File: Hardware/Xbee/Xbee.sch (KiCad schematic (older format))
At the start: 39 parts, among them J1 Alimentación, J2 Raspberry, J3 Pines 1, J4 Pines 2, J5 Programación, J6 Entrada, J7 Salida, K1 Rele12V, Q2 BC338, Q3 BC338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

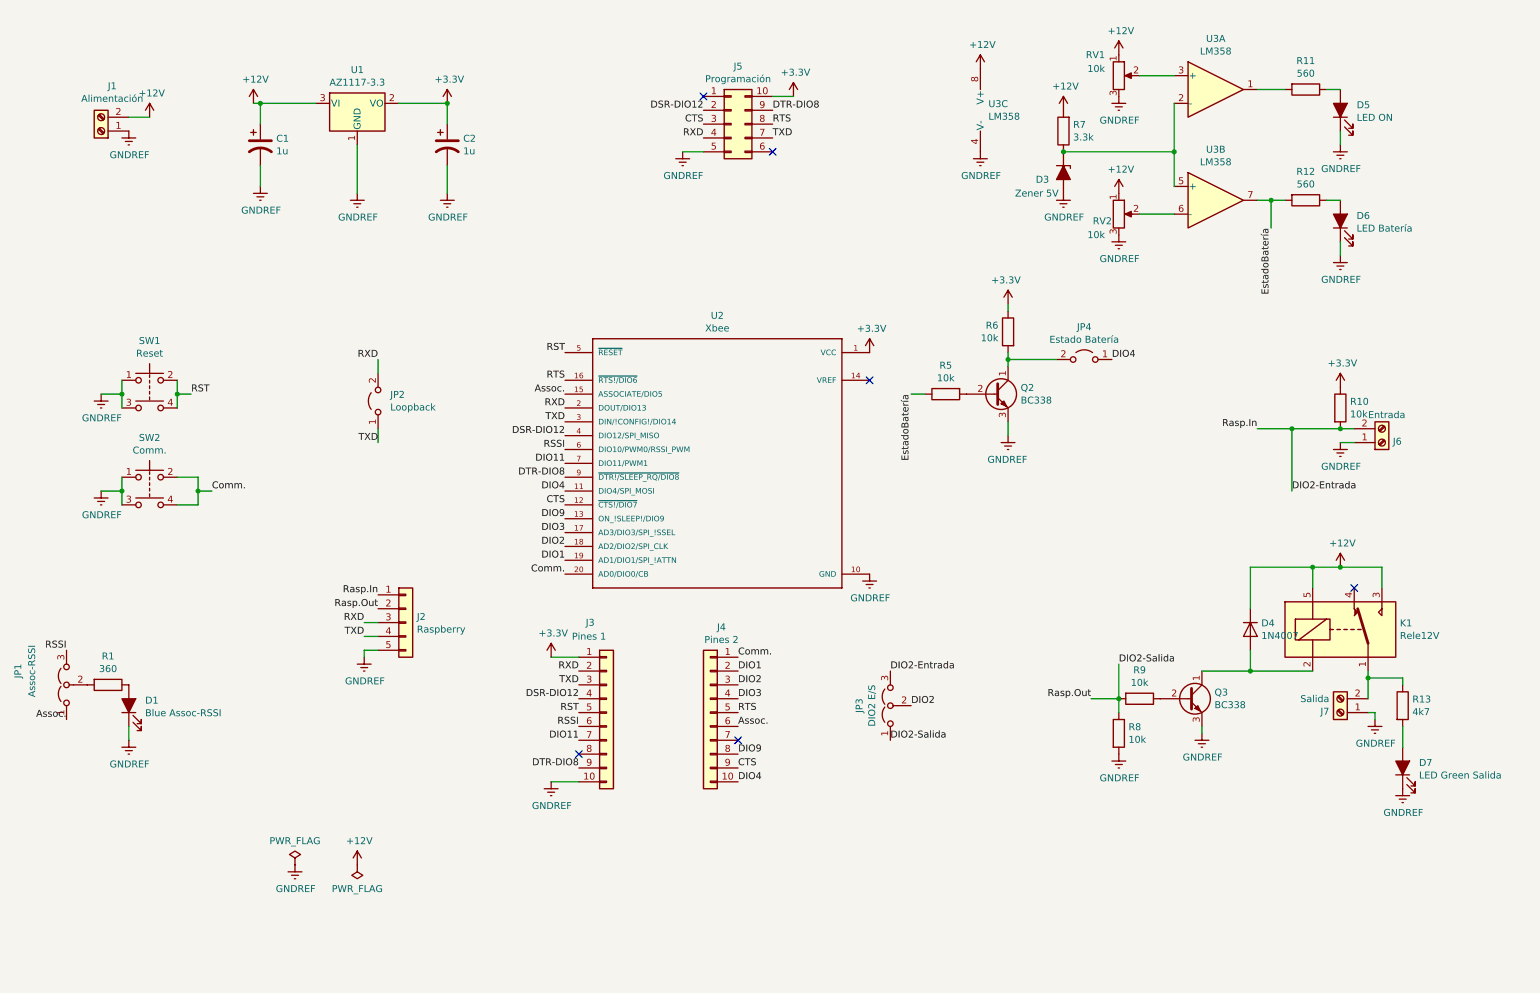
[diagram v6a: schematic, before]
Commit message: MOSFET, R SMD
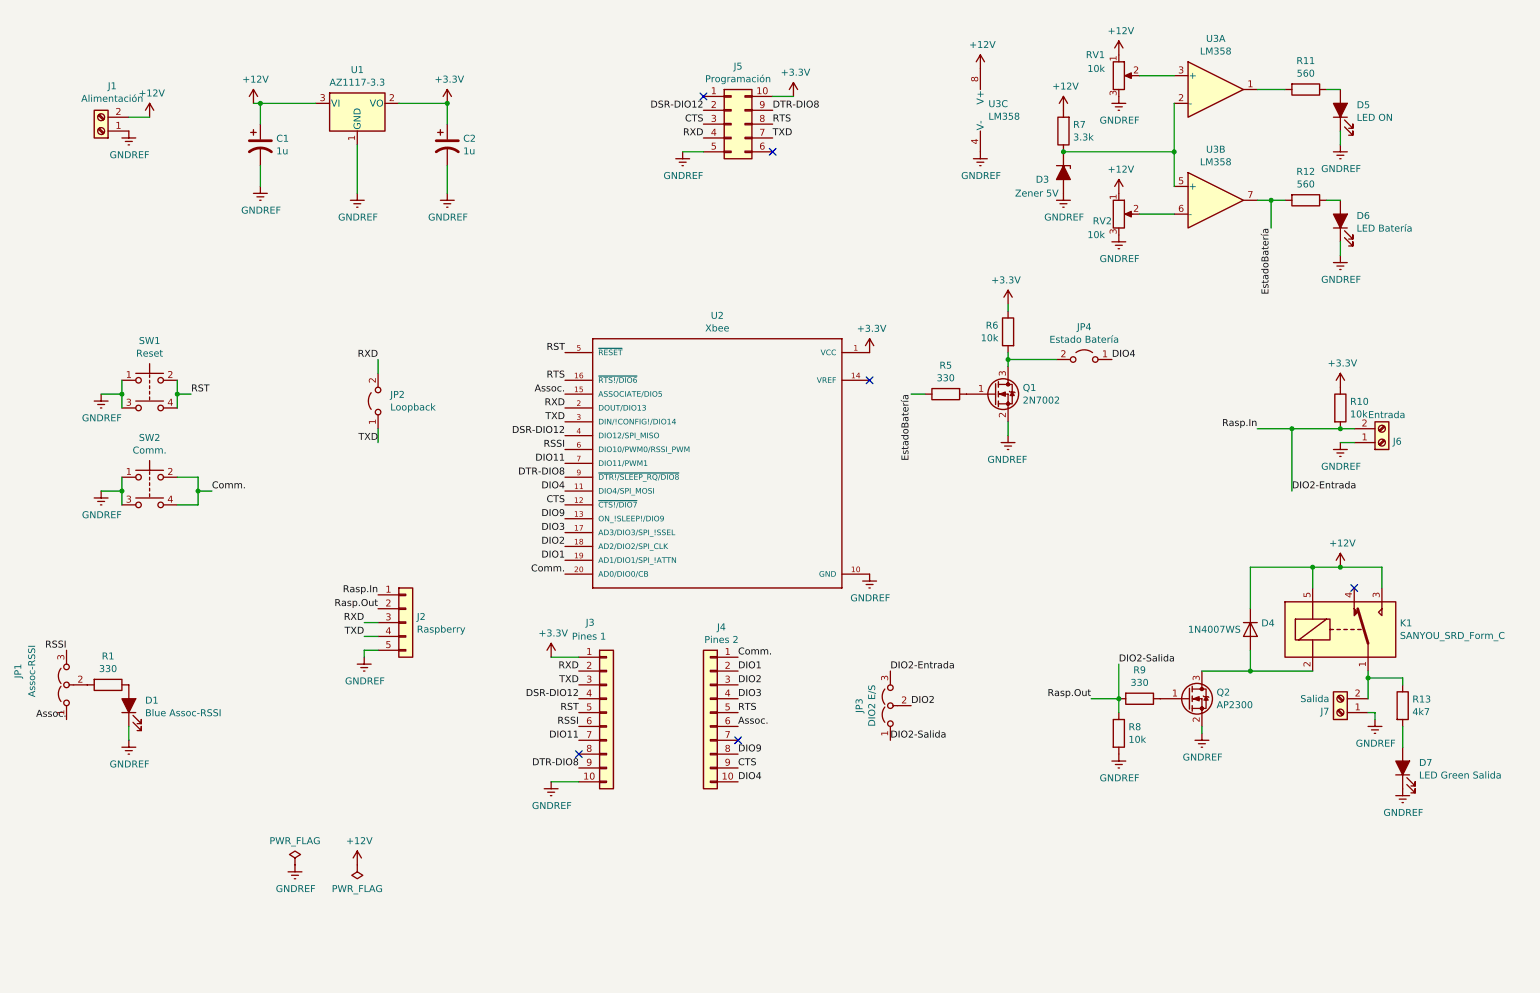
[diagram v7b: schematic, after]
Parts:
- removed K1: Rele12V, Relay_THT:Relay_SPDT_SANYOU_SRD_Series_Form_C, symbol Xbee-rescue:DIPxx-1Cxx-51x-Relay
- removed Q2, Q3: BC338, Package_TO_SOT_THT:TO-92_Inline, symbol Xbee-rescue:BC338-Transistor_BJT
- added K1: SANYOU_SRD_Form_C, Relay_THT:Relay_SPDT_SANYOU_SRD_Series_Form_C, symbol Relay:SANYOU_SRD_Form_C
- added Q1: 2N7002, Package_TO_SOT_SMD:SOT-23, symbol Transistor_FET:2N7002
- added Q2: AP2300, Package_TO_SOT_SMD:SOT-23, symbol Transistor_FET:2N7002
- D4: value 1N4007 -> 1N4007WS; footprint Diode_THT:D_DO-41_SOD81_P10.16mm_Horizontal -> Diode_SMD:D_SOD-323_HandSoldering
- R1: value 360 -> 330; footprint Resistor_THT:R_Axial_DIN0207_L6.3mm_D2.5mm_P10.16mm_Horizontal -> Resistor_SMD:R_0805_2012Metric_Pad1.15x1.40mm_HandSolder
- R10, R11, R12, R13, R6, R7, R8: footprint Resistor_THT:R_Axial_DIN0207_L6.3mm_D2.5mm_P10.16mm_Horizontal -> Resistor_SMD:R_0805_2012Metric_Pad1.15x1.40mm_HandSolder
- R5, R9: value 10k -> 330; footprint Resistor_THT:R_Axial_DIN0207_L6.3mm_D2.5mm_P10.16mm_Horizontal -> Resistor_SMD:R_0805_2012Metric_Pad1.15x1.40mm_HandSolder
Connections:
- net +12V: now also K1.3, K1.5
- net GNDREF: now also Q1.2 (S), Q2.2 (S)
- net at D4.2 (A): now also K1.2, Q2.3 (D)
- net at J7.2 (Pin_2), R13.1: now also K1.1
- net at JP4.2 (B), R6.2: now also Q1.3 (D)
- net at R5.2: now also Q1.1 (G)
- net at R9.1: now also Q2.1 (G)
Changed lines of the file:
@@
 P 1250 5500
 F 0 "R1" V 1043 5500 50  0000 C CNN
-F 1 "360" V 1134 5500 50  0000 C CNN
-F 2 "Resistor_THT:R_Axial_DIN0207_L6.3mm_D2.5mm_P10.16mm_Horizontal" V 1180 5500 50  0001 C CNN
+F 1 "330" V 1134 5500 50  0000 C CNN
+F 2 "Resistor_SMD:R_0805_2012Metric_Pad1.15x1.40mm_HandSolder" V 1180 5500 50  0001 C CNN
 F 3 "~" H 1250 5500 50  0001 C CNN
 	1    1250 5500
@@
 F 0 "R7" H 8080 1454 50  0000 R CNN
 F 1 "3.3k" H 8080 1545 50  0000 R CNN
-F 2 "Resistor_THT:R_Axial_DIN0207_L6.3mm_D2.5mm_P10.16mm_Horizontal" V 8080 1500 50  0001 C CNN
+F 2 "Resistor_SMD:R_0805_2012Metric_Pad1.15x1.40mm_HandSolder" V 8080 1500 50  0001 C CNN
 F 3 "~" H 8150 1500 50  0001 C CNN
 	1    8150 1500
@@
 F 0 "R11" V 9693 1200 50  0000 C CNN
 F 1 "560" V 9784 1200 50  0000 C CNN
-F 2 "Resistor_THT:R_Axial_DIN0207_L6.3mm_D2.5mm_P10.16mm_Horizontal" V 9830 1200 50  0001 C CNN
+F 2 "Resistor_SMD:R_0805_2012Metric_Pad1.15x1.40mm_HandSolder" V 9830 1200 50  0001 C CNN
 F 3 "~" H 9900 1200 50  0001 C CNN
 	1    9900 1200
@@
 F 0 "R12" V 9693 2000 50  0000 C CNN
 F 1 "560" V 9784 2000 50  0000 C CNN
-F 2 "Resistor_THT:R_Axial_DIN0207_L6.3mm_D2.5mm_P10.16mm_Horizontal" V 9830 2000 50  0001 C CNN
+F 2 "Resistor_SMD:R_0805_2012Metric_Pad1.15x1.40mm_HandSolder" V 9830 2000 50  0001 C CNN
 F 3 "~" H 9900 2000 50  0001 C CNN
 	1    9900 2000
@@
 $EndComp
 $Comp
-L Xbee-rescue:BC338-Transistor_BJT Q2
-U 1 1 5C1B14D4
-P 7650 3400
-F 0 "Q2" H 7841 3446 50  0000 L CNN
-F 1 "BC338" H 7841 3355 50  0000 L CNN
-F 2 "Package_TO_SOT_THT:TO-92_Inline" H 7850 3325 50  0001 L CIN
-F 3 "http://diotec.com/tl_files/diotec/files/pdf/datasheets/bc337" H 7650 3400 50  0001 L CNN
-	1    7650 3400
-	1    0    0    -1
-$EndComp
-$Comp
 L Xbee-rescue:+3.3V-power #PWR023
 U 1 1 5C1B1DFA
@@
 F 0 "R6" H 7820 2996 50  0000 L CNN
 F 1 "10k" H 7820 2905 50  0000 L CNN
-F 2 "Resistor_THT:R_Axial_DIN0207_L6.3mm_D2.5mm_P10.16mm_Horizontal" V 7680 2950 50  0001 C CNN
+F 2 "Resistor_SMD:R_0805_2012Metric_Pad1.15x1.40mm_HandSolder" V 7680 2950 50  0001 C CNN
 F 3 "~" H 7750 2950 50  0001 C CNN
 	1    7750 2950
@@
 P 7300 3400
 F 0 "R5" V 7093 3400 50  0000 C CNN
-F 1 "10k" V 7184 3400 50  0000 C CNN
-F 2 "Resistor_THT:R_Axial_DIN0207_L6.3mm_D2.5mm_P10.16mm_Horizontal" V 7230 3400 50  0001 C CNN
+F 1 "330" V 7184 3400 50  0000 C CNN
+F 2 "Resistor_SMD:R_0805_2012Metric_Pad1.15x1.40mm_HandSolder" V 7230 3400 50  0001 C CNN
 F 3 "~" H 7300 3400 50  0001 C CNN
 	1    7300 3400
@@
 F 0 "R10" H 10220 3546 50  0000 L CNN
 F 1 "10k" H 10220 3455 50  0000 L CNN
-F 2 "Resistor_THT:R_Axial_DIN0207_L6.3mm_D2.5mm_P10.16mm_Horizontal" V 10080 3500 50  0001 C CNN
+F 2 "Resistor_SMD:R_0805_2012Metric_Pad1.15x1.40mm_HandSolder" V 10080 3500 50  0001 C CNN
 F 3 "~" H 10150 3500 50  0001 C CNN
 	1    10150 3500
@@
 $EndComp
 $Comp
-L Xbee-rescue:BC338-Transistor_BJT Q3
-U 1 1 5C1D025D
-P 9050 5600
-F 0 "Q3" H 9241 5646 50  0000 L CNN
-F 1 "BC338" H 9241 5555 50  0000 L CNN
-F 2 "Package_TO_SOT_THT:TO-92_Inline" H 9250 5525 50  0001 L CIN
-F 3 "http://diotec.com/tl_files/diotec/files/pdf/datasheets/bc337" H 9050 5600 50  0001 L CNN
-	1    9050 5600
-	1    0    0    -1
-$EndComp
-$Comp
 L Xbee-rescue:R-Device R9
 U 1 1 5C1D0264
 P 8700 5600
 F 0 "R9" V 8493 5600 50  0000 C CNN
-F 1 "10k" V 8584 5600 50  0000 C CNN
-F 2 "Resistor_THT:R_Axial_DIN0207_L6.3mm_D2.5mm_P10.16mm_Horizontal" V 8630 5600 50  0001 C CNN
+F 1 "330" V 8584 5600 50  0000 C CNN
+F 2 "Resistor_SMD:R_0805_2012Metric_Pad1.15x1.40mm_HandSolder" V 8630 5600 50  0001 C CNN
 F 3 "~" H 8700 5600 50  0001 C CNN
 	1    8700 5600
@@
 	1    0    0    -1
 $EndComp
-$Comp
-L Xbee-rescue:DIPxx-1Cxx-51x-Relay K1
-U 1 1 5C1D5DE1
-P 10150 5100
-F 0 "K1" H 10580 5146 50  0000 L CNN
-F 1 "Rele12V" H 10580 5055 50  0000 L CNN
-F 2 "Relay_THT:Relay_SPDT_SANYOU_SRD_Series_Form_C" H 10600 5050 50  0001 L CNN
-F 3 "https://standexelectronics.com/wp-content/uploads/datasheet_reed_relay_DIP.pdf" H 10150 5100 50  0001 C CNN
-	1    10150 5100
-	1    0    0    -1
-$EndComp
 Wire Wire Line
 	9950 4800 9950 4650
@@
 F 0 "R13" H 10670 5696 50  0000 L CNN
 F 1 "4k7" H 10670 5605 50  0000 L CNN
-F 2 "Resistor_THT:R_Axial_DIN0207_L6.3mm_D2.5mm_P10.16mm_Horizontal" V 10530 5650 50  0001 C CNN
+F 2 "Resistor_SMD:R_0805_2012Metric_Pad1.15x1.40mm_HandSolder" V 10530 5650 50  0001 C CNN
 F 3 "~" H 10600 5650 50  0001 C CNN
 	1    10600 5650
@@
 P 9500 5100
 F 0 "D4" V 9454 5179 50  0000 L CNN
-F 1 "1N4007" V 9545 5179 50  0000 L CNN
-F 2 "Diode_THT:D_DO-41_SOD81_P10.16mm_Horizontal" H 9500 4925 50  0001 C CNN
+F 1 "1N4007WS" V 9500 4650 50  0000 L CNN
+F 2 "Diode_SMD:D_SOD-323_HandSoldering" H 9500 4925 50  0001 C CNN
 F 3 "http://www.vishay.com/docs/88503/1n4001.pdf" H 9500 5100 50  0001 C CNN
 	1    9500 5100
@@
 F 0 "R8" H 8620 5896 50  0000 L CNN
 F 1 "10k" H 8620 5805 50  0000 L CNN
-F 2 "Resistor_THT:R_Axial_DIN0207_L6.3mm_D2.5mm_P10.16mm_Horizontal" V 8480 5850 50  0001 C CNN
+F 2 "Resistor_SMD:R_0805_2012Metric_Pad1.15x1.40mm_HandSolder" V 8480 5850 50  0001 C CNN
 F 3 "~" H 8550 5850 50  0001 C CNN
 	1    8550 5850
@@
 Wire Wire Line
 	3050 1600 3050 1950
+$Comp
+L Transistor_FET:2N7002 Q1
+U 1 1 5D728B89
+P 7650 3400
+F 0 "Q1" H 7856 3446 50  0000 L CNN
+F 1 "2N7002" H 7856 3355 50  0000 L CNN
+F 2 "Package_TO_SOT_SMD:SOT-23" H 7850 3325 50  0001 L CIN
+F 3 "https://www.fairchildsemi.com/datasheets/2N/2N7002.pdf" H 7650 3400 50  0001 L CNN
+	1    7650 3400
+	1    0    0    -1
+$EndComp
+$Comp
+L Transistor_FET:2N7002 Q2
+U 1 1 5D75E2ED
+P 9050 5600
+F 0 "Q2" H 9256 5646 50  0000 L CNN
+F 1 "AP2300" H 9256 5555 50  0000 L CNN
+F 2 "Package_TO_SOT_SMD:SOT-23" H 9250 5525 50  0001 L CIN
+F 3 "https://www.fairchildsemi.com/datasheets/2N/2N7002.pdf" H 9050 5600 50  0001 L CNN
+	1    9050 5600
+	1    0    0    -1
+$EndComp
+$Comp
+L Relay:SANYOU_SRD_Form_C K1
+U 1 1 5D884156
+P 10150 5100
+F 0 "K1" H 10580 5146 50  0000 L CNN
+F 1 "SANYOU_SRD_Form_C" H 10580 5055 50  0000 L CNN
+F 2 "Relay_THT:Relay_SPDT_SANYOU_SRD_Series_Form_C" H 10600 5050 50  0001 L CNN
+F 3 "http://www.sanyourelay.ca/public/products/pdf/SRD.pdf" H 10150 5100 50  0001 C CNN
+	1    10150 5100
+	1    0    0    -1
+$EndComp
 $EndSCHEMATC

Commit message: Sheets-Text
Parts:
- removed C1, C2: 1u, Capacitor_SMD:C_0805_2012Metric, symbol Xbee-rescue:CP1-Device
- removed U1: AZ1117-3.3, Package_TO_SOT_SMD:SOT-223-3_TabPin2, symbol Regulator_Linear:AZ1117-3.3
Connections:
- net LED-Assoc-RSSI: now reaches JP1.2 (C), R1.2
- net Bobina: now reaches D4.2 (A), K1.2, Q2.3 (D)
- net Salida-Rele: now reaches J7.2 (Pin_2), K1.1, R13.1
- net Bat-DIO4: now reaches JP4.2 (B), Q1.3 (D), R6.2
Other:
- note added: "Borneras-Entrada-Salida"
- note added: "Botones"
- note added: "Circuito-Salida"
- note added: "Estado-Batería"
- note added: "Jumper-Prog"
- note added: "LED's Indicadores"
- note added: "Lectura-Estado-Bateria"
- moved on the sheet: D1, D3, D4, D5, D6, D7, J1, J2, J3, J4, J5, J6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
